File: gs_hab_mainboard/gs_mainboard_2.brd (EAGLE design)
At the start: 72.7 x 59 mm, 40 parts, among them IC1 LM4040/385 (2.5V), IC2 LM358D, J2 Storm Det, J6 LF Comm, J7 HF Comm, J8 Weather stat., J9 Ext 5V, Q1 BSS138, Q2 BSS138, Q3 BSS138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

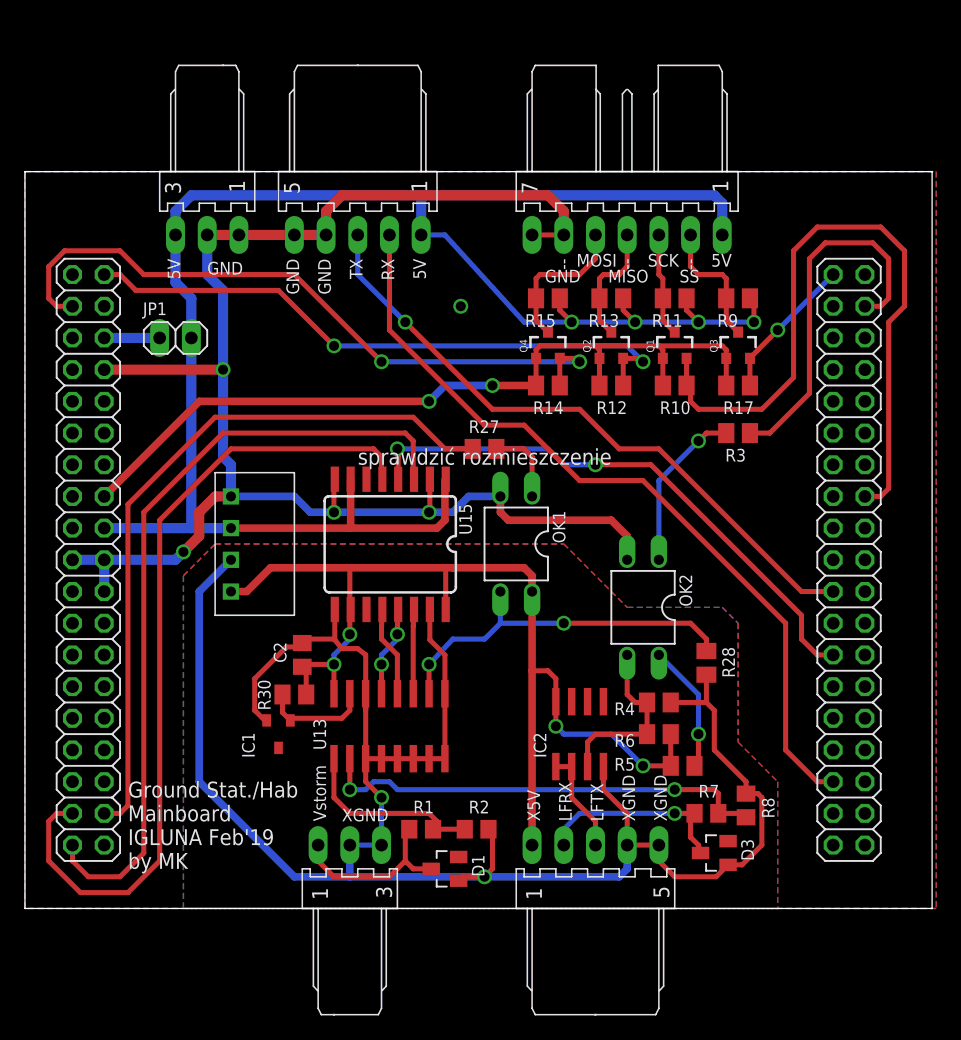
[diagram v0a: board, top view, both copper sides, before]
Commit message: updated lib, corrected boards (after printing)
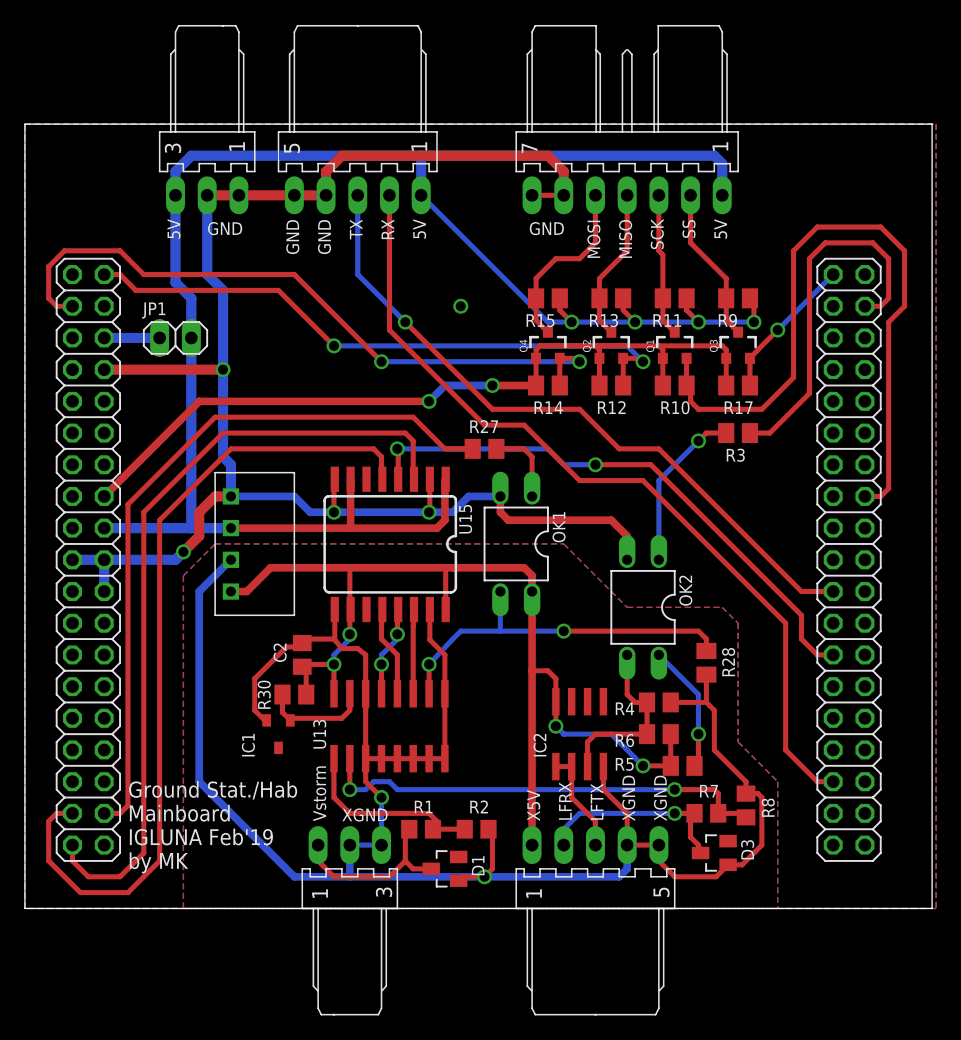
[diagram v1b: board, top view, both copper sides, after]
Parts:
- moved J7 3.17 mm to (26.7, 57.1)
- moved J8 3.17 mm to (48.3, 57.1)
- moved J9 3.17 mm to (14.6, 57.1)
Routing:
- net +5V: track 149.8 -> 154.1 mm
- net GND: track 127.8 -> 131.0 mm
- net USART1_TX: track 51.8 -> 55.0 mm
- net USART1_RX: track 64.1 -> 67.3 mm
- net SPI3_SCK_EXT: track 8.32 -> 11.5 mm
- net SPI3_MOSI_EXT: track 12.0 -> 14.4 mm
- net SPI3_MISO_EXT: track 9.85 -> 12.3 mm
- net SPI3_SS_EXT: track 10.5 -> 12.5 mm
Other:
- board size 72.7 x 59 mm -> 72.7 x 62.9 mm
- board text removed: "--"

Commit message: final, after another review
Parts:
- J8: value Weather stat. -> Weather st.
- moved IC2 1.27 mm to (44.5, 15.2)
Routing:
- net GND1: track 163.0 -> 164.3 mm
- net LF_TX: track 8.35 -> 9.62 mm
- net VEE: track 85.8 -> 86.7 mm
